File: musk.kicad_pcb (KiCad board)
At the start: 2 copper layers, 104 x 106.5 mm, 89 parts, among them J1 debug-port, J10 Conn_01x06_Male, J2 USB_C_Receptacle_USB2.0, J3 Conn_01x06_Male, J4 Conn_01x06_Male, J5 Conn_01x06_Male, J6 Conn_01x06_Male, J7 Conn_01x06_Male, J8 Conn_01x06_Male, J9 Conn_01x06_Male, K1 diode-choc, K10 diode-choc, K11 diode-choc, K12 diode-choc, K13 diode-choc, K14 diode-choc, K15 diode-choc, K16 diode-choc, K2 diode-choc, K3 diode-choc, K4 diode-choc, K5 diode-choc, K6 diode-choc, K7 diode-choc, K8 diode-choc, K9 diode-choc, Q1 BC807, SW1 SW_Push, SW2 RotaryEncoder, U1 MT25QL128ABA1ESE, U10 LM397, U2 ms88sf3-nrf52840, U3 LSM6DS3, U4 XC6220B331MR, U6 SRV05-4, U8 PMW3610, U9 MCP1804x-1802xMB

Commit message: done
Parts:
- removed SC1: solar, misc:KXOB25-05X3F
- added BT1: li-ion, Connector_JST:JST_PH_S2B-PH-SM4-TB_1x02-1MP_P2.00mm_Horizontal, F.Cu at (130.5, 105.4)
- added C16: 1u, Capacitor_SMD:C_0603_1608Metric, F.Cu at (106.4, 99.4)
- added G***: LOGO, LOGO, B.Cu at (128.7, 88.9)
- added JP2: left right or all, Jumper:SolderJumper-3_P1.3mm_Open_RoundedPad1.0x1.5mm, F.Cu at (84.3, 78.4)
- added K17: diode-choc, pg1232:pg1232-DC, B.Cu at (95.1, 20.7)
- added REF**: feet, misc:nothing, F.Cu at (71.1, 90.6)
- added REF**: wheel-hole, MountingHole:MountingHole_2.2mm_M2, F.Cu at (73.9, 80.2)
- added REF**: feet, misc:nothing, F.Cu at (104.5, 45.0)
- added REF**: mouse, misc:nothing, F.Cu at (121.4, 50.7)
- added REF**: wheel-hole, MountingHole:MountingHole_2.2mm_M2, F.Cu at (70.8, 73.7)
- added REF**: sensor ring, misc:nothing, F.Cu at (110.9, 85.7)
- added REF**: feet, misc:nothing, F.Cu at (150.5, 54.5)
- added REF**: crides-pos, misc:crides-pos, B.Cu at (114.4, 103.8)
- added REF**: feet, misc:nothing, F.Cu at (153.9, 90.6)
- added REF**: feet, misc:nothing, F.Cu at (71.2, 50.0)
- added REF**: feet, misc:nothing, F.Cu at (121.5, 114.5)
- J10, J3: moved to F.Cu
- J9: moved to B.Cu
- JP1: value All or none -> left right or all
- K13: footprint pg1232:pg1232-DSS -> pg1232:pg1232-DC
- R24: value 2.8k -> ?
- moved K13 75.0 mm to (69.6, 90.7), turned to 90 degrees
- moved SW1 73.8 mm to (74.2, 20.7), turned to 0 degrees
- moved JP1 45.2 mm to (80.7, 78.4), turned to -90 degrees
- moved U4 11.2 mm to (109.2, 99.7), turned to 180 degrees
- moved R4 7.71 mm to (67.3, 80.8)
- moved K15 6.74 mm to (141.8, 20.7), turned to 90 degrees
- moved D2 5.96 mm to (95.2, 20.7), turned to 90 degrees
- moved R5 5.95 mm to (68.8, 80.8)
- moved C4 5.88 mm to (130.5, 109.3), turned to 180 degrees
- moved R6 5.42 mm to (70.3, 80.8)
- moved C10 5.30 mm to (99.9, 92.0), turned to 90 degrees
- moved K16 5.26 mm to (107.6, 20.7), turned to -90 degrees
- moved K14 5.07 mm to (82.1, 90.7), turned to 90 degrees
- moved REF** 4.90 mm to (121.4, 78.7)
- moved R2 4.61 mm to (81.0, 83.0)
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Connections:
- C5 pad 2: /power/SOLAR -> SOLAR
- J10 pad 1: Net-(J10-Pad1) -> Net-(J7-Pad6)
- J10 pad 2: Net-(J10-Pad2) -> Net-(J7-Pad5)
- J10 pad 3: Net-(J10-Pad3) -> Net-(J7-Pad4)
- J10 pad 4: unconnected-(J10-Pad4) -> Net-(J7-Pad3)
- J10 pad 5: Net-(J10-Pad5) -> Net-(J7-Pad2)
- J3 pad 5: Net-(J3-Pad5) -> Net-(J6-Pad2)
- J3 pad 6: Net-(J3-Pad6) -> Net-(J6-Pad1)
- J5 pad 1: C0 -> RST
- J5 pad 2: R3 -> GND
- J6 pad 1: Net-(J3-Pad1) -> Net-(J6-Pad1)
- J6 pad 2: Net-(J3-Pad2) -> Net-(J6-Pad2)
- J6 pad 3: Net-(J3-Pad3) -> Net-(J3-Pad4)
- J6 pad 4: Net-(J3-Pad4) -> Net-(J3-Pad3)
- J6 pad 5: Net-(J3-Pad5) -> Net-(J3-Pad2)
- J6 pad 6: Net-(J3-Pad6) -> Net-(J3-Pad1)
- J7 pad 1: Net-(J10-Pad1) -> Net-(J10-Pad6)
- J7 pad 2: Net-(J10-Pad2) -> Net-(J7-Pad2)
- J7 pad 3: Net-(J10-Pad3) -> Net-(J7-Pad3)
- J7 pad 4: unconnected-(J7-Pad4) -> Net-(J7-Pad4)
- J7 pad 5: Net-(J10-Pad5) -> Net-(J7-Pad5)
- J7 pad 6: Net-(J10-Pad6) -> Net-(J7-Pad6)
- J8 pad 3: R3 -> C4
- J8 pad 4: unconnected-(J8-Pad4) -> R3
- J8 pad 5: SOLAR -> unconnected-(J8-Pad5)
- J8 pad 6: GND -> unconnected-(J8-Pad6)
- J9 pad 2: Net-(J9-Pad2) -> unconnected-(J9-Pad2)
- J9 pad 4: unconnected-(J9-Pad4) -> Net-(K17-Pad2)
- J9 pad 5: Net-(J9-Pad5) -> Net-(K16-Pad2)
- J9 pad 6: Net-(J9-Pad6) -> unconnected-(J9-Pad6)
- JP1 pad 1: +3V3 -> 3V3_nRF
- JP1 pad 2: SOLAR_OUT -> +3V3
- K13 pad 1: Net-(J3-Pad2) -> R3
- K13 pad 2: Net-(J3-Pad1) -> C0
- K15 pad 1: Net-(J10-Pad3) -> Net-(J7-Pad4)
- K15 pad 2: Net-(J10-Pad1) -> Net-(J10-Pad6)
- K16 pad 2: Net-(J9-Pad2) -> Net-(K16-Pad2)
- L2 pad 1: /power/SOLAR -> SOLAR
- R13 pad 1: /power/SOLAR -> SOLAR
- SW1 pad 1: Net-(SW1-Pad1) -> Net-(J6-Pad1)
- SW1 pad 2: GND -> Net-(J6-Pad2)
- U2 pad 15: ~{BLUE} -> ~{RED}
- U2 pad 17: ~{RED} -> ~{BLUE}
- U2 pad 28: Net-(SW1-Pad1) -> RST
- U2 pad 32: SOLAR_OUT -> VDDH
- U2 pad 40: unconnected-(U2-Pad40) -> R3
- U2 pad 41: R3 -> C4
- U7 pad 2: /power/SOLAR -> SOLAR
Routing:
- net C4: track 0.00 -> 48.7 mm, vias 0 -> 2
- net Net-(J7-Pad4): track 0.00 -> 46.2 mm
- net Net-(J10-Pad1): track 46.0 -> 0.00 mm
- net +3V3: track 92.8 -> 50.1 mm, vias 4 -> 3
- net Net-(SW1-Pad1): track 42.1 -> 0.00 mm, vias 2 -> 0
- net Net-(K17-Pad2): track 0.00 -> 40.1 mm
- net RST: track 0.00 -> 36.3 mm, vias 0 -> 1
- net Net-(J10-Pad3): track 36.0 -> 0.00 mm
- net Net-(J6-Pad2): track 0.00 -> 35.2 mm
- net Net-(J7-Pad3): track 0.00 -> 34.6 mm
- net Net-(J6-Pad1): track 0.00 -> 34.1 mm
- net Net-(J3-Pad5): track 33.4 -> 0.00 mm
- net Net-(J7-Pad5): track 0.00 -> 33.2 mm
- net 3V3_LDO: track 4.32 -> 37.4 mm, vias 0 -> 2
- net Net-(J10-Pad5): track 33.0 -> 0.00 mm
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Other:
- board size 104 x 106.5 mm -> 104 x 106 mm
- board text added: "MoUSe with Keys"
- board text added: "github.com/crides"
- board text added: "musk"

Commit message: 5 thumb cluster
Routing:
- net C2: track 148.7 -> 135.7 mm
- net GND: vias 46 -> 48

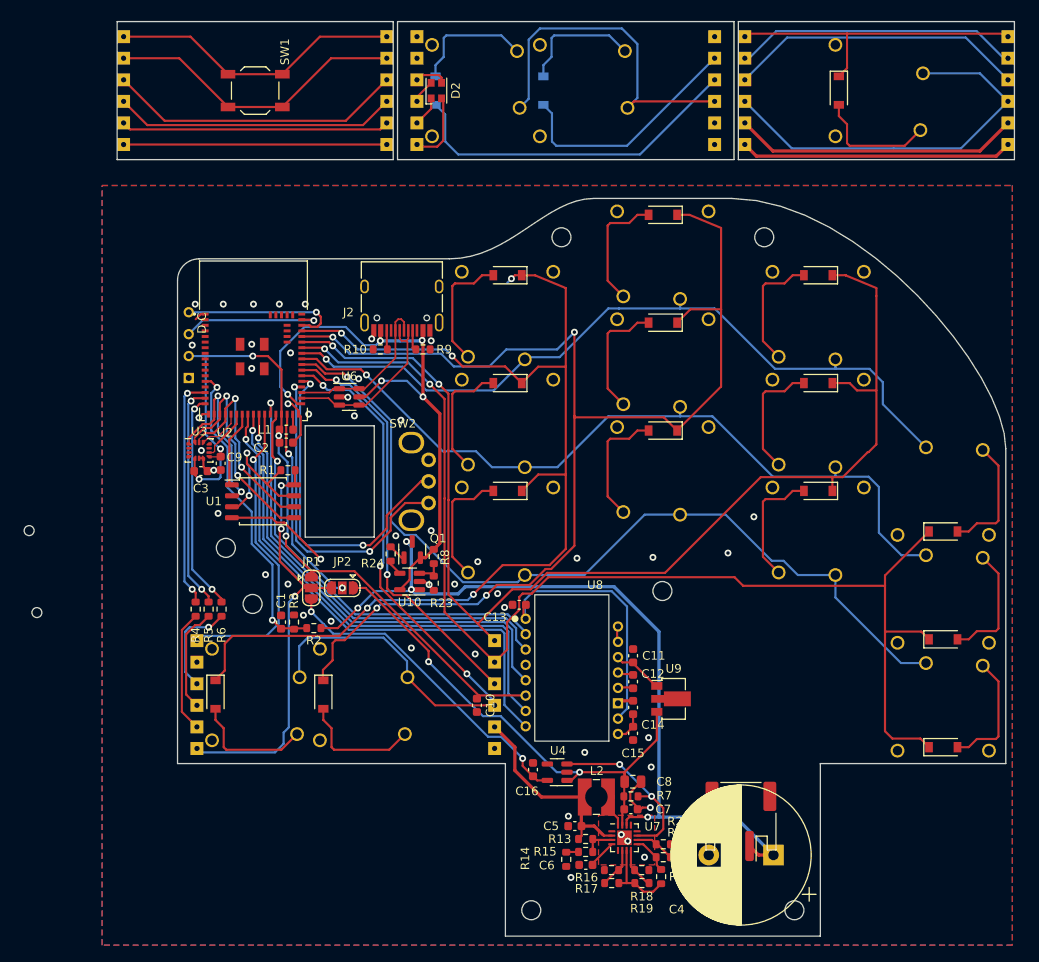
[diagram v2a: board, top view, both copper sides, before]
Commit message: hotswap choc mini
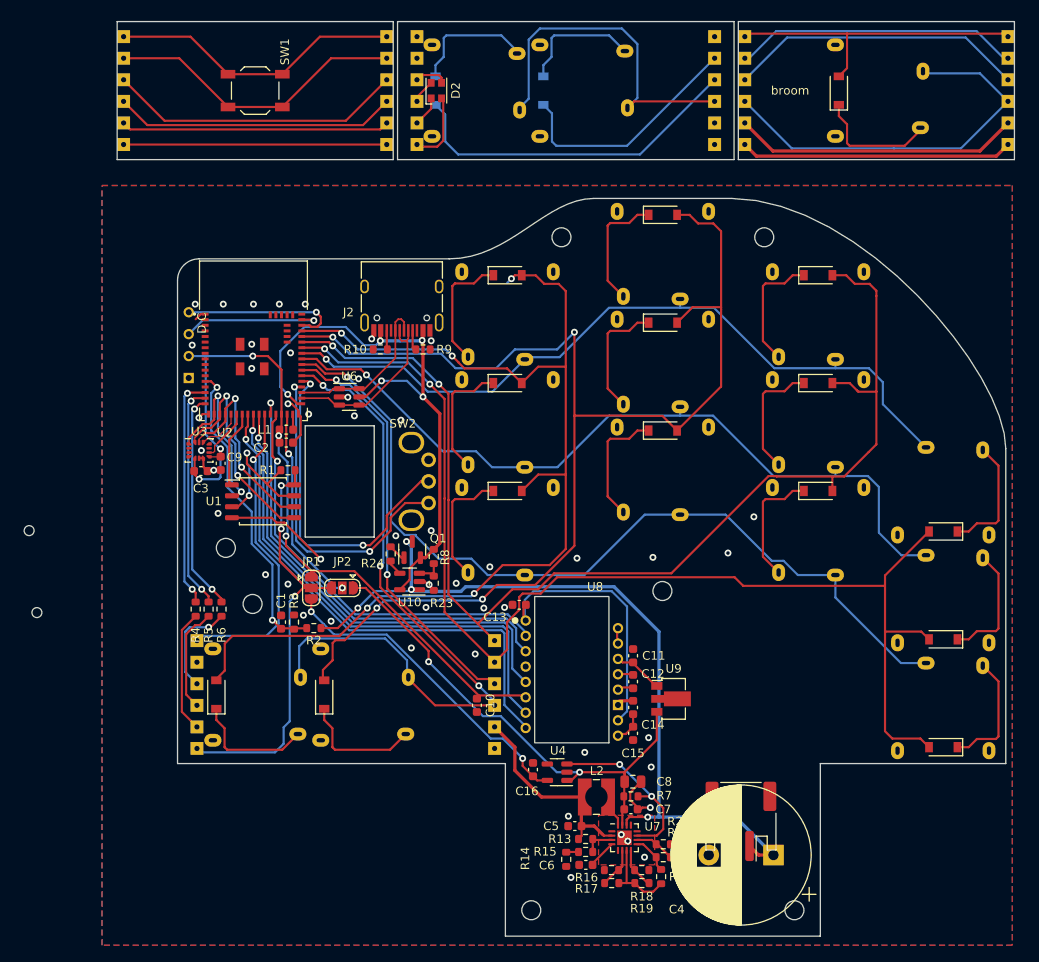
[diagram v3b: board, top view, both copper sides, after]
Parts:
- K1, K5, K9: footprint pg1232:pg1232-DCR -> pg1232:pg1232-DHCR
- K10, K13, K14, K15, K16, K17, K2, K6: footprint pg1232:pg1232-DC -> pg1232:pg1232-DHC
- K11, K3, K7: footprint pg1232:pg1232-DCL -> pg1232:pg1232-DHCL
- K12, K4, K8: footprint pg1232:pg1232-DCN -> pg1232:pg1232-DHCN
- moved REF** 17.1 mm to (121.3, 131.5)
- moved U8 0.20 mm to (110.9, 86.4)
- moved K13 0.10 mm to (69.7, 90.7)
- moved K14 0.10 mm to (82.2, 90.7)
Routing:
- net R2: track 101.5 -> 100.9 mm
- net GND: track 35.0 -> 34.9 mm, vias 48 -> 49
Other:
- board text added: "both"
- board text added: "broom"
- board text added: "no mask"

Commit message: backup
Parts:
- moved REF** 109.0 mm to (155.9, 87.4)
- moved REF** 43.6 mm to (69.7, 42.9)
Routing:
- net 3V3_nRF: track 91.2 -> 86.6 mm
- net SCLK2: track 52.7 -> 52.1 mm
- net GND: vias 49 -> 50
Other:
- outline, holes or cut-outs redrawn

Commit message: swap bms and reg
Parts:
- removed C1: 10nF, Capacitor_SMD:C_0603_1608Metric
- removed C8: 4.7uF, Capacitor_SMD:C_0805_2012Metric
- removed Q1: BC807, Package_TO_SOT_SMD:SOT-23
- removed R15: 5.9M, Resistor_SMD:R_0603_1608Metric
- removed R16, R17, R18, R19: 5.1M, Resistor_SMD:R_0603_1608Metric
- removed R20: 1M, Resistor_SMD:R_0603_1608Metric
- removed R21: 4.12M, Resistor_SMD:R_0603_1608Metric
- removed R22: 4.87M, Resistor_SMD:R_0603_1608Metric
- removed R23: 8.2k, Resistor_SMD:R_0603_1608Metric
- removed R24: ?, Resistor_SMD:R_0603_1608Metric
- removed U10: LM397, Package_TO_SOT_SMD:SOT-23-5
- removed U9: MCP1804x-1802xMB, Package_TO_SOT_SMD:SOT-89-3
- added D1: RED, LED_SMD:LED_0805_2012Metric, F.Cu at (125.2, 26.0)
- added R11: 1k, Resistor_SMD:R_0603_1608Metric, F.Cu at (97.2, 83.1)
- added R12: 100k, Resistor_SMD:R_0603_1608Metric, F.Cu at (115.1, 103.8)
- added U5: BQ24072, Package_DFN_QFN:VQFN-16-1EP_3x3mm_P0.5mm_EP1.68x1.68mm_ThermalVias, F.Cu at (91.7, 73.6)
- C12: value 100uF -> 100nF
- C4: value Li Cap -> 4.7uF; footprint Capacitor_THT:CP_Radial_D16.0mm_P7.50mm -> Capacitor_SMD:C_0603_1608Metric
- C6: value 10nF -> 4.7uF
- C7: value 0.1uF -> 10uF
- L2: value 22uH -> 2.2uH; footprint Inductor_SMD:L_Wuerth_WE-TPC-3816 -> Inductor_SMD:L_1008_2520Metric
- R13: value 4.12M -> 100k
- R14: value 10M -> 100k
- R2, R3: value 5.1M -> 100k
- R7: value 1M -> 10k
- R8: value 2.8k -> 10k
- U1: value MT25QL128ABA1ESE -> W25Q128
- U7: value ~ -> TLV62568DBV; footprint Package_DFN_QFN:QFN-16-1EP_3x3mm_P0.5mm_EP1.7x1.7mm -> Package_TO_SOT_SMD:SOT-23-5
- moved C4 51.5 mm to (90.6, 76.7)
- moved C6 41.6 mm to (94.6, 72.9), turned to 90 degrees
- moved C5 38.8 mm to (88.8, 74.3), turned to 90 degrees
- moved C16 35.3 mm to (80.7, 75.3)
- moved U4 35.0 mm to (83.6, 75.9)
- moved R7 34.4 mm to (94.4, 77.3), turned to -90 degrees
- moved BT1 17.3 mm to (129.3, 88.2), turned to 0 degrees
- moved U7 9.52 mm to (109.2, 101.9), turned to 180 degrees
- moved R14 5.47 mm to (109.8, 104.4), turned to 180 degrees
- moved C7 5.06 mm to (112.8, 103.0), turned to 0 degrees
- moved R3 5.02 mm to (73.7, 81.9), turned to 180 degrees
- moved R2 4.45 mm to (76.7, 81.9)
- moved R8 3.24 mm to (92.9, 77.3), turned to -90 degrees
- moved R13 2.31 mm to (112.8, 105.2), turned to 180 degrees
- moved L2 1.78 mm to (113.3, 100.9), turned to 0 degrees
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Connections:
- C4 pad 1: BAT -> VBUS
- C5 pad 2: SOLAR -> VDDH_OUT
- C6 pad 1: GND -> BAT
- C6 pad 2: Net-(C6-Pad2) -> GND
- C7 pad 2: SOLAR_OUT -> +1V8
- J8 pad 5: unconnected-(J8-Pad5) -> VDDH_OUT
- J8 pad 6: unconnected-(J8-Pad6) -> Net-(J8-Pad6)
- J9 pad 1: unconnected-(J9-Pad1) -> Net-(D1-Pad1)
- J9 pad 2: unconnected-(J9-Pad2) -> Net-(D1-Pad2)
- JP2 pad 1: SOLAR_OUT -> VDDH_OUT
- L2 pad 1: SOLAR -> Net-(L2-Pad1)
- L2 pad 2: Net-(L2-Pad2) -> +1V8
- R13 pad 1: SOLAR -> Net-(R12-Pad2)
- R14 pad 2: Net-(R14-Pad2) -> Net-(R13-Pad2)
- R3 pad 2: GND -> BAT_MEAS_EN
- R7 pad 2: SOLAR_OUT -> GND
- R8 pad 2: VBUS -> GND
- U2 pad 14: unconnected-(U2-Pad14) -> BAT_MEAS_EN
- U4 pad 1: SOLAR_OUT -> VDDH_OUT
- U4 pad 3: Net-(R7-Pad1) -> VDDH_OUT
- U7 pad 1: GND -> VDDH_OUT
- U7 pad 2: SOLAR -> GND
- U7 pad 3: Net-(R13-Pad2) -> Net-(L2-Pad1)
- U7 pad 4: Net-(C6-Pad2) -> VDDH_OUT
- U7 pad 5: GND -> Net-(R13-Pad2)
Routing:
- net SOLAR_OUT: track 58.6 -> 0.00 mm, vias 2 -> 0
- net VDDH_OUT: track 0.00 -> 57.9 mm, vias 0 -> 3
- net BAT_MEAS_EN: track 0.00 -> 35.2 mm, vias 0 -> 2
- net BAT: track 94.8 -> 59.8 mm, vias 4 -> 3
- net 3V3_LDO: track 37.4 -> 10.1 mm
- net SOLAR: track 24.0 -> 0.00 mm
- net Net-(R7-Pad1): track 20.6 -> 2.64 mm, vias 2 -> 0
- net +1V8: track 6.25 -> 23.2 mm
- net ~{CHG}: track 0.00 -> 15.5 mm, vias 0 -> 2
- net Net-(J8-Pad6): track 0.00 -> 14.0 mm, vias 0 -> 1
- net Net-(R17-Pad2): track 9.48 -> 0.00 mm
- net Net-(R18-Pad2): track 4.58 -> 0.00 mm
- net Net-(R16-Pad2): track 4.58 -> 0.00 mm
- net Net-(R21-Pad2): track 4.54 -> 0.00 mm
- net Net-(R20-Pad1): track 4.39 -> 0.00 mm
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- added copper zone on F.Cu, net BAT
- added copper zone on F.Cu, net VDDH_OUT
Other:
- board size 104 x 106 mm -> 106 x 105 mm
- board text added: "JLCJLCJLCJLC"

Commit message: top
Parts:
- removed the REF** at (156.0, 65.0)
- moved REF** 29.3 mm to (91.3, 56.5)
- moved G*** 3.83 mm to (127.5, 92.0)
- moved R3 3.78 mm to (71.8, 78.6)
- moved R2 3.76 mm to (74.9, 78.6)
- moved R4 2.20 mm to (66.5, 77.9)
- moved R5 2.20 mm to (68.0, 77.9)
- moved R6 2.20 mm to (69.5, 77.9)
- moved BT1 2.05 mm to (127.2, 88.2)
- moved REF** 1.30 mm to (115.0, 103.1)
- moved R11 1.10 mm to (97.2, 82.0)
- moved REF** 1.03 mm to (84.0, 90.0)
- moved REF** 0.90 mm to (71.0, 73.0)
- moved REF** 0.89 mm to (110.2, 85.2)
- moved REF** 0.74 mm to (120.7, 50.5)
- moved REF** 0.54 mm to (153.7, 90.1)
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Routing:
- net VBUS: track 71.1 -> 59.1 mm, vias 7 -> 6
- net BAT_MEAS_EN: track 35.2 -> 28.9 mm
- net BAT_MEAS: track 33.6 -> 31.1 mm
- net ~{BLUE}: track 25.1 -> 22.6 mm
- net ~{RED}: track 26.5 -> 24.2 mm
- net ~{GREEN}: track 25.6 -> 23.5 mm
- net Net-(J5-Pad5): track 14.2 -> 16.4 mm
- net BAT: track 59.8 -> 62.0 mm
- net C0: track 126.4 -> 124.3 mm, vias 5 -> 4
- net Net-(J5-Pad4): track 12.2 -> 14.1 mm
- net R1: track 91.9 -> 93.3 mm
- net GND: track 38.2 -> 39.6 mm, vias 39 -> 41
- net +3V3: track 50.3 -> 49.0 mm
- net VDDH: track 23.3 -> 24.5 mm
- net VDDH_OUT: track 57.9 -> 56.8 mm
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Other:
- outline, holes or cut-outs redrawn

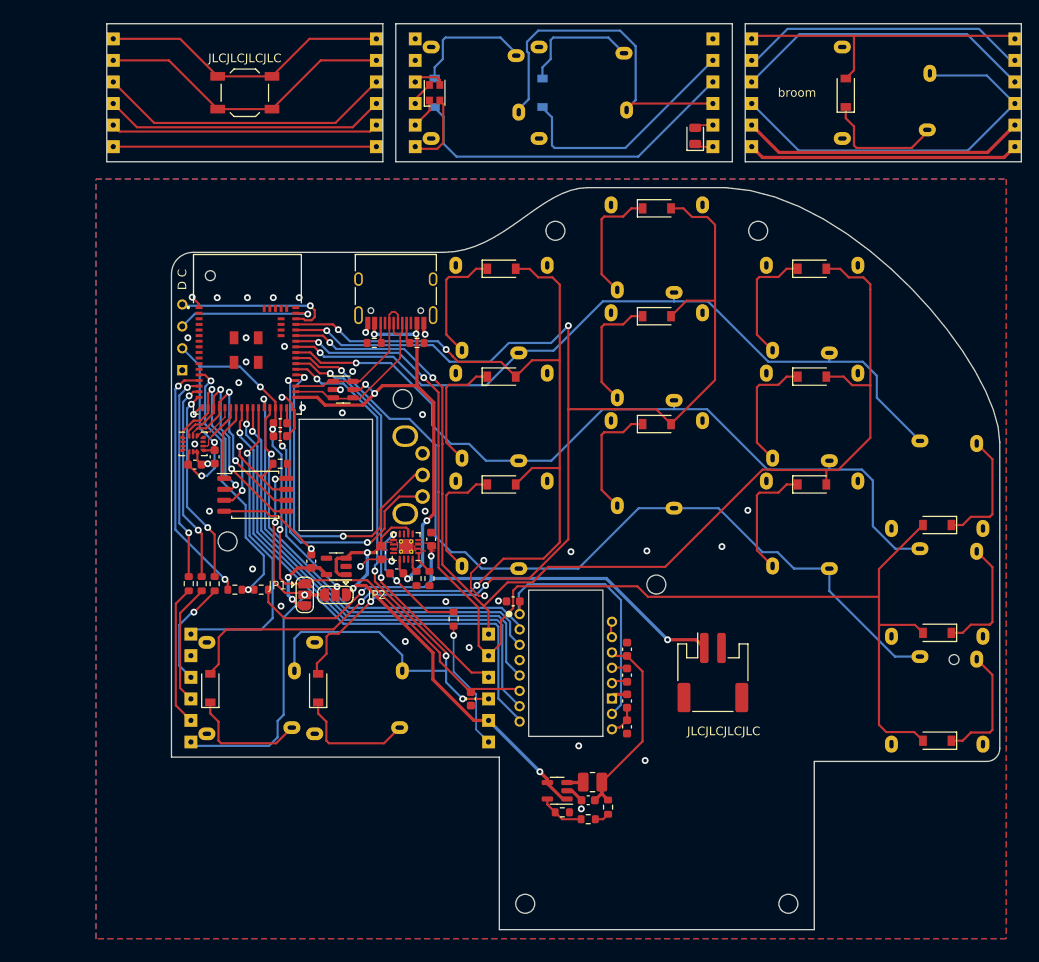
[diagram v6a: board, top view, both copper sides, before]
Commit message: adjust position
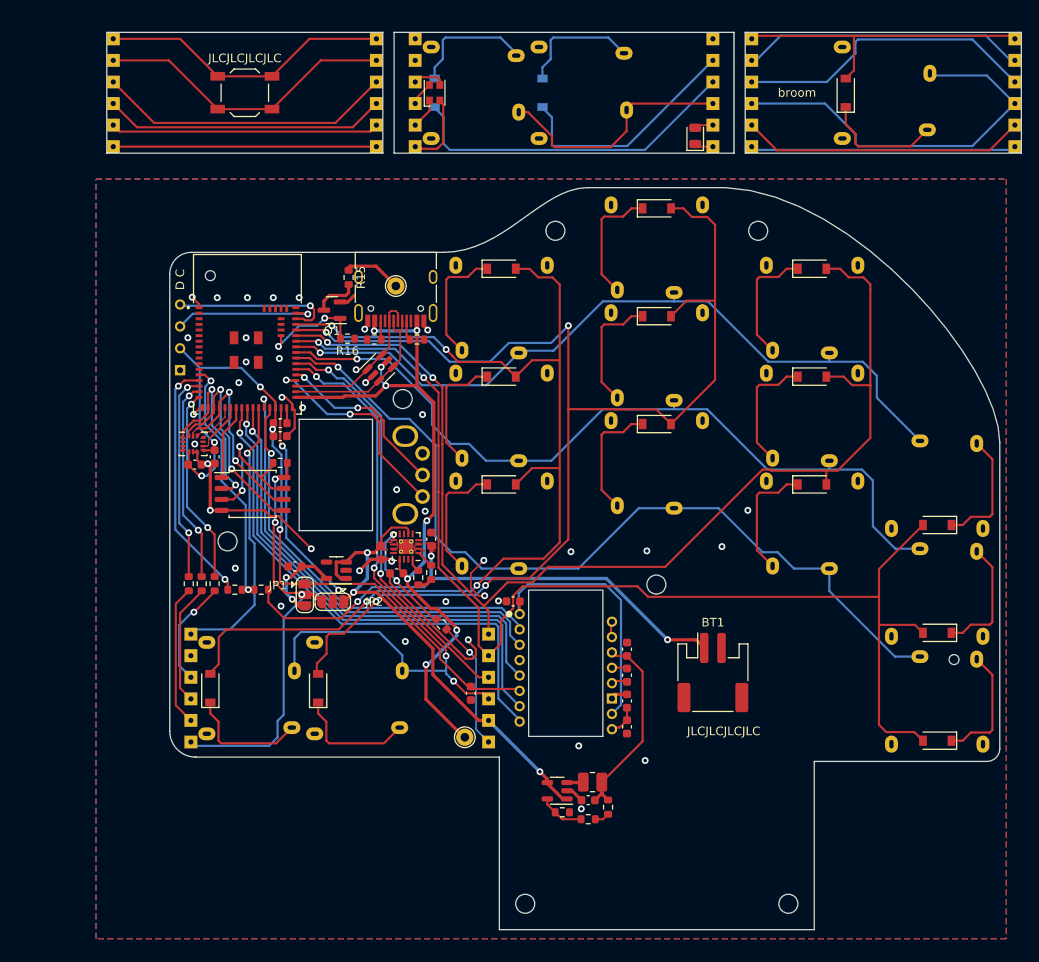
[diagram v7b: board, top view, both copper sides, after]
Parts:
- added Q1: AO3400A, Package_TO_SOT_SMD:SOT-23, F.Cu at (83.1, 46.2)
- added R15: 100, Resistor_SMD:R_0603_1608Metric, F.Cu at (85.0, 42.4)
- added R16: 1M, Resistor_SMD:R_0603_1608Metric, F.Cu at (84.9, 49.5)
- added TP1: LED+, TestPoint:TestPoint_THTPad_D2.0mm_Drill1.0mm, F.Cu at (98.5, 95.7)
- added TP2: LED-, TestPoint:TestPoint_THTPad_D2.0mm_Drill1.0mm, F.Cu at (90.5, 43.4)
- J10, J3, J4, J5, J6, J7, J8, J9: value Conn_01x06_Male -> bridge
- U1: value W25Q128 -> W25Q128JVS
- moved U6 4.97 mm to (88.7, 52.9), turned to 45 degrees
- moved C16 1.99 mm to (78.8, 75.9), turned to 180 degrees
- moved R11 1.52 mm to (95.8, 82.6), turned to -45 degrees
- moved JP2 0.85 mm to (83.2, 80.0)
- moved R7 0.73 mm to (94.6, 76.6)
- moved C10 0.65 mm to (99.2, 90.6)
- moved U4 0.45 mm to (83.6, 76.3)
- moved R9 0.40 mm to (93.0, 49.6)
- moved R10 0.40 mm to (88.0, 49.6)
- moved U1 0.32 mm to (73.9, 67.5)
- moved J2 0.25 mm to (90.5, 43.4)
- moved J1 0.25 mm to (65.5, 49.4)
- moved R8 0.22 mm to (93.1, 77.2)
- moved R1 0.10 mm to (77.1, 63.9), turned to 0 degrees
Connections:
- R1 pad 1: +3V3 -> Net-(R1-Pad1)
- R1 pad 2: Net-(R1-Pad2) -> +3V3
- U1 pad 3: Net-(R1-Pad2) -> Net-(R1-Pad1)
- U1 pad 7: Net-(R1-Pad2) -> Net-(R1-Pad1)
- U2 pad 60: unconnected-(U2-Pad60) -> ~{LED_OFF}
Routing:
- net GND: track 39.6 -> 67.9 mm
- net VBUS: track 59.1 -> 82.7 mm, vias 6 -> 8
- net Net-(R1-Pad2): track 18.2 -> 0.00 mm, vias 2 -> 0
- net B: track 38.7 -> 20.6 mm
- net Net-(R1-Pad1): track 0.00 -> 18.1 mm, vias 0 -> 2
- net (no net): track 0.00 -> 14.0 mm
- net A: track 37.7 -> 24.7 mm
- net Net-(J9-Pad3): track 40.7 -> 28.4 mm
- net ~{LED_OFF}: track 0.00 -> 12.2 mm, vias 0 -> 2
- net Net-(R15-Pad1): track 0.00 -> 6.80 mm
- net Net-(Q1-Pad3): track 0.00 -> 5.28 mm
- net RST: track 36.4 -> 32.5 mm
- net ~{CHG}: track 15.0 -> 13.5 mm
- net BAT_MEAS: track 31.1 -> 29.6 mm
- net VDDH: track 24.5 -> 25.6 mm
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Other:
- board size 106 x 105 mm -> 106 x 104 mm
